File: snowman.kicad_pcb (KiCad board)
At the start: 2 copper layers, 38.4 x 70.7 mm, 13 parts, among them SW1 SW_SPST, SW2 SW_SPST, SW3 SW_SPST, U1 ATTINY85-20SU

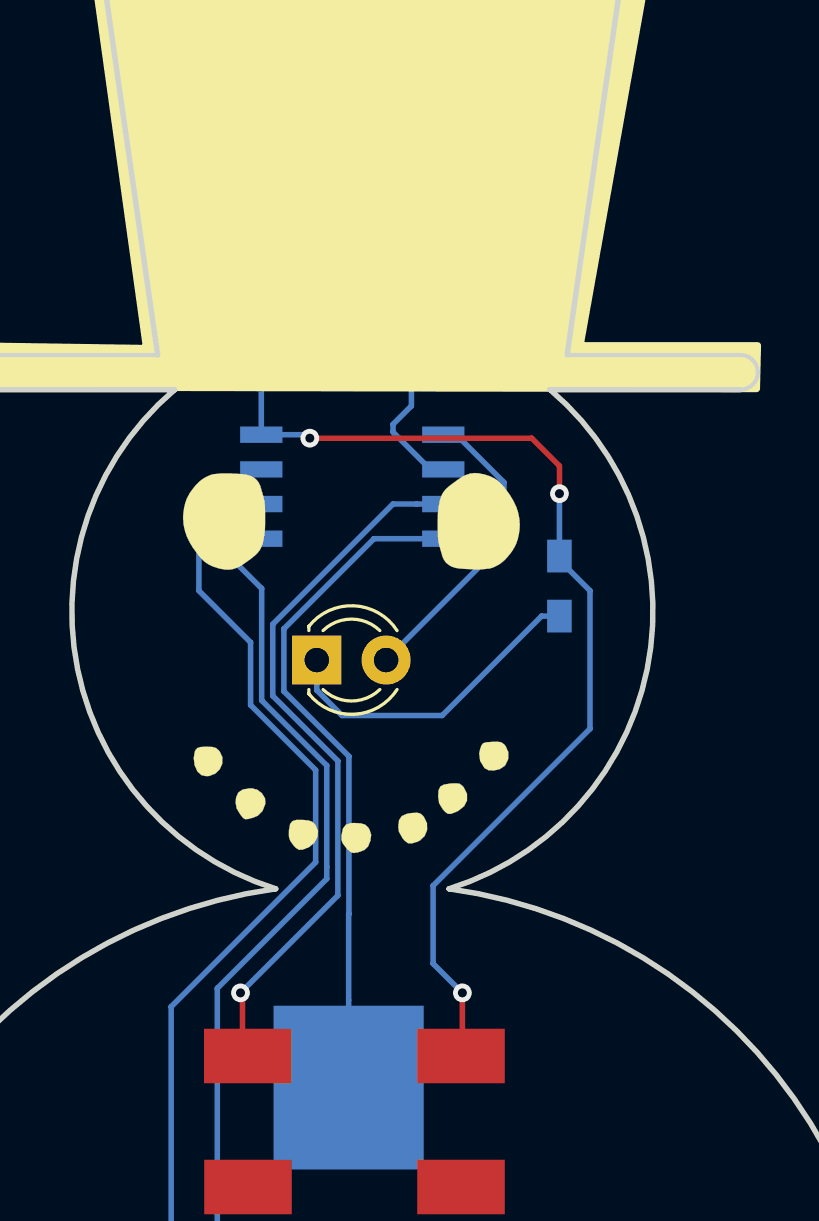
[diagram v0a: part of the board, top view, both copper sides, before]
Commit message: Update Footprints
Update piezo buzzer footprint, making it wider for easier hand soldering.
Update button schematic to change pin 2 to pin 4 to match buttons being used
Update LED footprint in schematic to 3mm
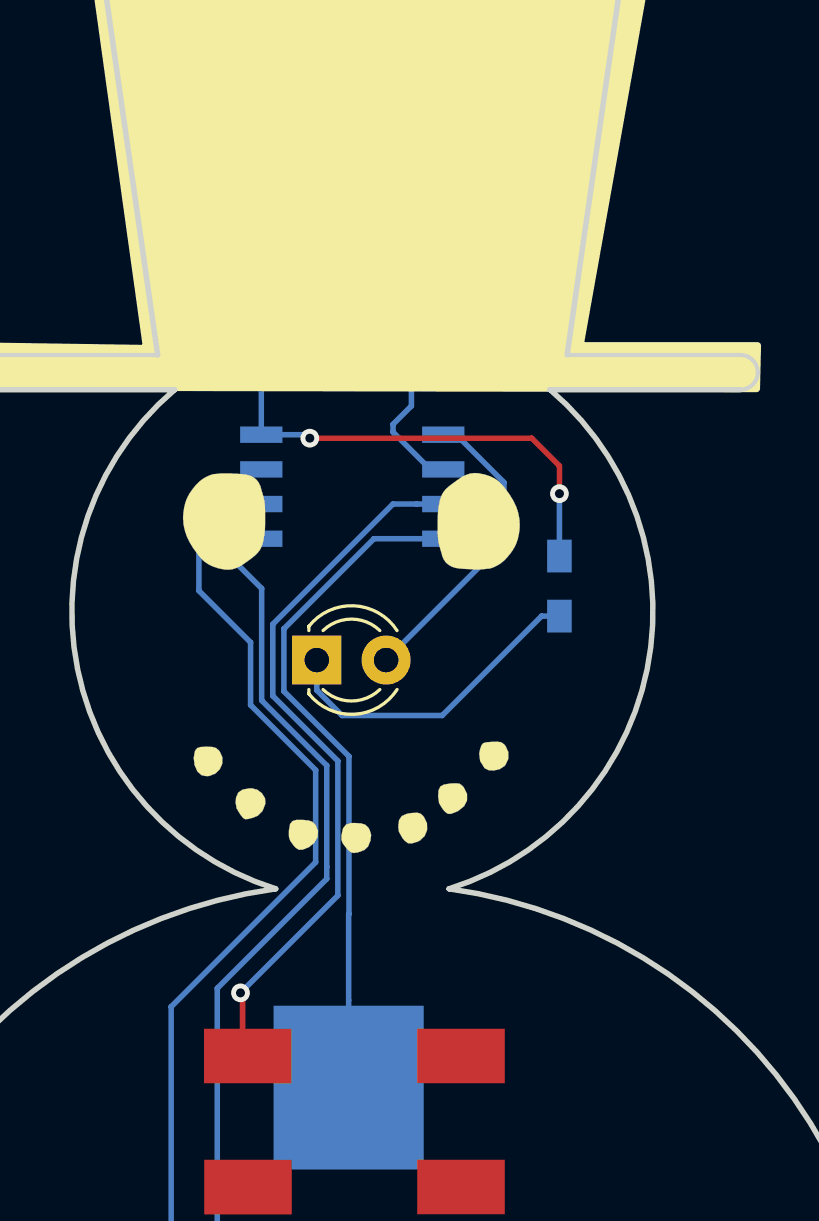
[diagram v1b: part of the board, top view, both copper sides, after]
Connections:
- SW1 pad 2: GND -> (no net)
- SW1 pad 4: (no net) -> GND
- SW2 pad 2: GND -> (no net)
- SW2 pad 4: (no net) -> GND
- SW3 pad 2: GND -> (no net)
- SW3 pad 4: (no net) -> GND
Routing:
- net GND: track 56.9 -> 35.4 mm, vias 5 -> 4
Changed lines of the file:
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@@
     (thickness 1.6)
     (drawings 18)
-    (tracks 91)
+    (tracks 84)
     (zones 0)
     (modules 13)
@@
     (add_net "Net-(U1-Pad1)")
   )
+  (module Piezo:Piezo-PKMCS0909E4000-R1 (layer F.Cu)
+    (at 160.02 60.706)
+    (fp_text reference PIEZO1 (at 0 -2.5908) (layer F.Fab)
+      (effects (font (size 1 1) (thickness 0.15)))
+    )
+    (fp_text value PIEZO (at 0 2.8448) (layer F.Fab)
+      (effects (font (size 1 1) (thickness 0.15)))
+    )
+    (pad 1 smd rect (at -3.89 -0.07) (size 1.4 3.2) (layers F.Cu F.Paste F.Mask)
+      (net 1 GND))
+    (pad 2 smd rect (at 4.49 -0.07) (size 1.4 3.2) (layers F.Cu F.Paste F.Mask)
+      (net 5 "Net-(PIEZO1-Pad2)"))
+  )
   (module ATTiny85:ATTiny85-20SU (layer B.Cu)
     (at 160.02 70.866)
@@
       (effects (font (size 1 1) (thickness 0.15)))
     )
-    (pad 4 smd rect (at 4.0124 2.3776) (size 3.2 2) (layers F.Cu F.Paste F.Mask))
+    (pad 4 smd rect (at 4.0124 2.3776) (size 3.2 2) (layers F.Cu F.Paste F.Mask)
+      (net 1 GND))
     (pad 3 smd rect (at -3.79 2.38) (size 3.2 2) (layers F.Cu F.Paste F.Mask))
-    (pad 2 smd rect (at 4.0124 -2.4224) (size 3.2 2) (layers F.Cu F.Paste F.Mask)
-      (net 1 GND))
+    (pad 2 smd rect (at 4.0124 -2.4224) (size 3.2 2) (layers F.Cu F.Paste F.Mask))
     (pad 1 smd rect (at -3.8 -2.42) (size 3.2 2) (layers F.Cu F.Paste F.Mask)
       (net 8 "Net-(SW3-Pad1)"))
@@
       (effects (font (size 1 1) (thickness 0.15)))
     )
-    (pad 4 smd rect (at 4.0124 2.3776) (size 3.2 2) (layers F.Cu F.Paste F.Mask))
+    (pad 4 smd rect (at 4.0124 2.3776) (size 3.2 2) (layers F.Cu F.Paste F.Mask)
+      (net 1 GND))
     (pad 3 smd rect (at -3.79 2.38) (size 3.2 2) (layers F.Cu F.Paste F.Mask))
-    (pad 2 smd rect (at 4.0124 -2.4224) (size 3.2 2) (layers F.Cu F.Paste F.Mask)
-      (net 1 GND))
+    (pad 2 smd rect (at 4.0124 -2.4224) (size 3.2 2) (layers F.Cu F.Paste F.Mask))
     (pad 1 smd rect (at -3.8 -2.42) (size 3.2 2) (layers F.Cu F.Paste F.Mask)
       (net 6 "Net-(SW1-Pad1)"))
@@
       (effects (font (size 1 1) (thickness 0.15)))
     )
-    (pad 4 smd rect (at 4.0124 2.3776) (size 3.2 2) (layers F.Cu F.Paste F.Mask))
+    (pad 4 smd rect (at 4.0124 2.3776) (size 3.2 2) (layers F.Cu F.Paste F.Mask)
+      (net 1 GND))
     (pad 3 smd rect (at -3.79 2.38) (size 3.2 2) (layers F.Cu F.Paste F.Mask))
-    (pad 2 smd rect (at 4.0124 -2.4224) (size 3.2 2) (layers F.Cu F.Paste F.Mask)
-      (net 1 GND))
+    (pad 2 smd rect (at 4.0124 -2.4224) (size 3.2 2) (layers F.Cu F.Paste F.Mask))
     (pad 1 smd rect (at -3.8 -2.42) (size 3.2 2) (layers F.Cu F.Paste F.Mask)
       (net 7 "Net-(SW2-Pad1)"))
@@
     )
   )
-  (module Piezo:Piezo-PKMCS0909E4000-R1 (layer F.Cu)
-    (at 160.02 60.706)
-    (fp_text reference PIEZO1 (at 0 -2.5908) (layer F.Fab)
-      (effects (font (size 1 1) (thickness 0.15)))
-    )
-    (fp_text value PIEZO (at 0 2.8448) (layer F.Fab)
-      (effects (font (size 1 1) (thickness 0.15)))
-    )
-    (pad 1 smd rect (at -3.7084 -0.0508) (size 1 3.2) (layers F.Cu F.Paste F.Mask)
-      (net 1 GND))
-    (pad 2 smd rect (at 4.3 -0.0508) (size 1 3.2) (layers F.Cu F.Paste F.Mask)
-      (net 5 "Net-(PIEZO1-Pad2)"))
-  )
   (module Resistors_SMD:R_0603_HandSoldering (layer B.Cu)
     (at 167.64 74.506 270)
@@
   )
   (segment (start 167.64 73.406) (end 167.64 73.556) (width 0.2032) (layer B.Cu) (net 1))
-  (segment (start 167.64 73.556) (end 168.76 74.676) (width 0.2032) (layer B.Cu) (net 1))
-  (segment (start 168.76 74.676) (end 168.76 79.735519) (width 0.2032) (layer B.Cu) (net 1))
-  (segment (start 168.76 79.735519) (end 163.012436 85.483083) (width 0.2032) (layer B.Cu) (net 1))
-  (segment (start 163.012436 85.483083) (end 163.012436 88.336436) (width 0.2032) (layer B.Cu) (net 1))
-  (segment (start 163.012436 88.336436) (end 164.084 89.408) (width 0.2032) (layer B.Cu) (net 1))
   (segment (start 157.988 61.468) (end 156.718 62.738) (width 0.2032) (layer B.Cu) (net 1))
   (segment (start 156.718 62.738) (end 156.718 68.961) (width 0.2032) (layer B.Cu) (net 1))
@@
   (via (at 167.64 71.12) (size 0.6858) (drill 0.3302) (layers F.Cu B.Cu) (net 1))
   (segment (start 158.496 69.088) (end 166.624 69.088) (width 0.2032) (layer F.Cu) (net 1))
-  (segment (start 164.084 89.408) (end 164.084 91.6684) (width 0.2032) (layer F.Cu) (net 1))
-  (segment (start 164.084 91.6684) (end 164.0324 91.72) (width 0.2032) (layer F.Cu) (net 1))
-  (via (at 164.084 89.408) (size 0.6858) (drill 0.3302) (layers F.Cu B.Cu) (net 1))
+  (segment (start 164.084 91.6684) (end 164.0324 91.72) (width 0.2032) (layer F.Cu) (net 0))
   (segment (start 156.718 68.961) (end 158.369 68.961) (width 0.2032) (layer B.Cu) (net 1))
   (segment (start 158.369 68.961) (end 158.496 69.088) (width 0.2032) (layer B.Cu) (net 1))

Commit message: Update Silkscreen
Add rev1 to date and board number silkscreen
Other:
- board text added: "15/06/2017 brd #03 rev1"
- board text removed: "15/06/2017 brd #03"
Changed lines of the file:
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@@
   (gr_arc (start 160.421436 75.436083) (end 157.246436 85.596083) (angle 122.4096183) (layer Edge.Cuts) (width 0.2))
   (gr_arc (start 159.786436 104.011083) (end 157.246436 85.596083) (angle -174.1142031) (layer Edge.Cuts) (width 0.2))
-  (gr_text "15/06/2017\nbrd #03" (at 143.914436 102.907083 90) (layer B.SilkS)
+  (gr_text "15/06/2017\nbrd #03 rev1" (at 143.914436 102.907083 90) (layer B.SilkS)
     (effects (font (size 0.75 0.75) (thickness 0.125)) (justify mirror))
   )

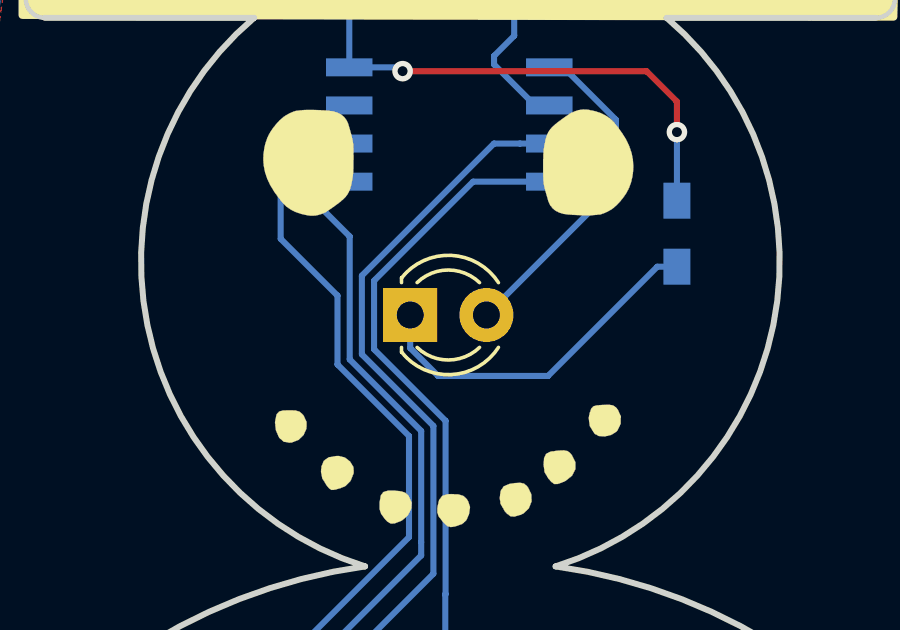
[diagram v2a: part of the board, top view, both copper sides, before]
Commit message: Remove Silk Screen From LED
Create new footprint for 3mm LED without silk screen
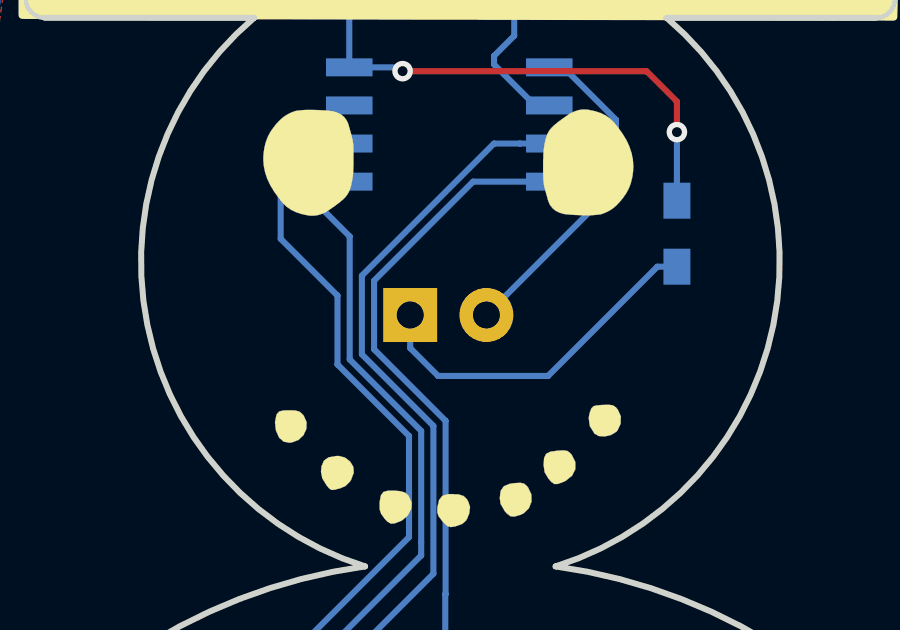
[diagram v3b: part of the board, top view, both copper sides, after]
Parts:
- D1: footprint LEDs:LED_D3.0mm -> nose:LED_D3.0mm_NoSilkS
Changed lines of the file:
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@@
-(kicad_pcb (version 20170123) (host pcbnew no-vcs-found-885a4c1~58~ubuntu16.04.1)
+(kicad_pcb (version 20170123) (host pcbnew no-vcs-found-0633d90~59~ubuntu16.04.1)
   (general
     (thickness 1.6)
@@
     (add_net "Net-(SW3-Pad1)")
     (add_net "Net-(U1-Pad1)")
+  )
+  (module nose:LED_D3.0mm_NoSilkS (layer F.Cu)
+    (at 158.75 77.216)
+    (descr "LED, diameter 3.0mm, 2 pins")
+    (tags "LED diameter 3.0mm 2 pins")
+    (fp_text reference D1 (at 1.27 -2.96) (layer F.Fab)
+      (effects (font (size 1 1) (thickness 0.15)))
+    )
+    (fp_text value LED (at 1.27 2.96) (layer F.Fab)
+      (effects (font (size 1 1) (thickness 0.15)))
+    )
+    (fp_arc (start 1.27 0) (end -0.23 -1.16619) (angle 284.3) (layer F.Fab) (width 0.1))
+    (fp_arc (start 1.27 0) (end -0.29 -1.235516) (angle 108.8) (layer F.Fab) (width 0.12))
+    (fp_arc (start 1.27 0) (end -0.29 1.235516) (angle -108.8) (layer F.Fab) (width 0.12))
+    (fp_arc (start 1.27 0) (end 0.229039 -1.08) (angle 87.9) (layer F.Fab) (width 0.12))
+    (fp_arc (start 1.27 0) (end 0.229039 1.08) (angle -87.9) (layer F.Fab) (width 0.12))
+    (fp_circle (center 1.27 0) (end 2.77 0) (layer F.Fab) (width 0.1))
+    (fp_line (start -0.23 -1.16619) (end -0.23 1.16619) (layer F.Fab) (width 0.1))
+    (fp_line (start -0.29 -1.236) (end -0.29 -1.08) (layer F.Fab) (width 0.12))
+    (fp_line (start -0.29 1.08) (end -0.29 1.236) (layer F.Fab) (width 0.12))
+    (fp_line (start -1.15 -2.25) (end -1.15 2.25) (layer F.CrtYd) (width 0.05))
+    (fp_line (start -1.15 2.25) (end 3.7 2.25) (layer F.CrtYd) (width 0.05))
+    (fp_line (start 3.7 2.25) (end 3.7 -2.25) (layer F.CrtYd) (width 0.05))
+    (fp_line (start 3.7 -2.25) (end -1.15 -2.25) (layer F.CrtYd) (width 0.05))
+    (pad 1 thru_hole rect (at 0 0) (size 1.8 1.8) (drill 0.9) (layers *.Cu *.Mask)
+      (net 4 "Net-(D1-Pad1)"))
+    (pad 2 thru_hole circle (at 2.54 0) (size 1.8 1.8) (drill 0.9) (layers *.Cu *.Mask)
+      (net 3 "Net-(D1-Pad2)"))
+    (model LEDs.3dshapes/LED_D3.0mm.wrl
+      (at (xyz 0 0 0))
+      (scale (xyz 0.393701 0.393701 0.393701))
+      (rotate (xyz 0 0 0))
+    )
   )
   (module Piezo:Piezo-PKMCS0909E4000-R1 (layer F.Cu)
@@
       (xy -0.283883 -1.748548) (xy -0.212089 -1.753827) (xy -0.117044 -1.756325) (xy -0.004867 -1.756281)) (layer F.SilkS) (width 0.01))
   )
-  (module LEDs:LED_D3.0mm (layer F.Cu)
-    (at 158.75 77.216)
-    (descr "LED, diameter 3.0mm, 2 pins")
-    (tags "LED diameter 3.0mm 2 pins")
-    (fp_text reference D1 (at 1.27 -2.96) (layer F.Fab)
-      (effects (font (size 1 1) (thickness 0.15)))
-    )
-    (fp_text value LED (at 1.27 2.96) (layer F.Fab)
-      (effects (font (size 1 1) (thickness 0.15)))
-    )
-    (fp_line (start 3.7 -2.25) (end -1.15 -2.25) (layer F.CrtYd) (width 0.05))
-    (fp_line (start 3.7 2.25) (end 3.7 -2.25) (layer F.CrtYd) (width 0.05))
-    (fp_line (start -1.15 2.25) (end 3.7 2.25) (layer F.CrtYd) (width 0.05))
-    (fp_line (start -1.15 -2.25) (end -1.15 2.25) (layer F.CrtYd) (width 0.05))
-    (fp_line (start -0.29 1.08) (end -0.29 1.236) (layer F.SilkS) (width 0.12))
-    (fp_line (start -0.29 -1.236) (end -0.29 -1.08) (layer F.SilkS) (width 0.12))
-    (fp_line (start -0.23 -1.16619) (end -0.23 1.16619) (layer F.Fab) (width 0.1))
-    (fp_circle (center 1.27 0) (end 2.77 0) (layer F.Fab) (width 0.1))
-    (fp_arc (start 1.27 0) (end 0.229039 1.08) (angle -87.9) (layer F.SilkS) (width 0.12))
-    (fp_arc (start 1.27 0) (end 0.229039 -1.08) (angle 87.9) (layer F.SilkS) (width 0.12))
-    (fp_arc (start 1.27 0) (end -0.29 1.235516) (angle -108.8) (layer F.SilkS) (width 0.12))
-    (fp_arc (start 1.27 0) (end -0.29 -1.235516) (angle 108.8) (layer F.SilkS) (width 0.12))
-    (fp_arc (start 1.27 0) (end -0.23 -1.16619) (angle 284.3) (layer F.Fab) (width 0.1))
-    (pad 2 thru_hole circle (at 2.54 0) (size 1.8 1.8) (drill 0.9) (layers *.Cu *.Mask)
-      (net 3 "Net-(D1-Pad2)"))
-    (pad 1 thru_hole rect (at 0 0) (size 1.8 1.8) (drill 0.9) (layers *.Cu *.Mask)
-      (net 4 "Net-(D1-Pad1)"))
-    (model LEDs.3dshapes/LED_D3.0mm.wrl
-      (at (xyz 0 0 0))
-      (scale (xyz 0.393701 0.393701 0.393701))
-      (rotate (xyz 0 0 0))
-    )
-  )
   (module Battery_Holders:Keystone_3002_1x2032-CoinCell (layer B.Cu)
